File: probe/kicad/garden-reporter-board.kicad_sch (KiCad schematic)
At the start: 29 parts, among them J1 70543-0106, J2 Conn_01x02, J3 70543-0002, J4 70543-0002, J5 70543-0002, Q1 Q_NMOS_SGD, Q2 Q_PMOS_SGD, U1 MCP1700-3302E_TO92, U2 MCP1700-3302E_TO92, U3 MCP1700-1202E_TO92

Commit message: Finish and verifiy routing, finish and verify BOM
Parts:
- J5: value 70543-0002 -> 70543-0106
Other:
- moved on the sheet: C11, C6, C7, J4, Q1, Q2, R3, R6, U2

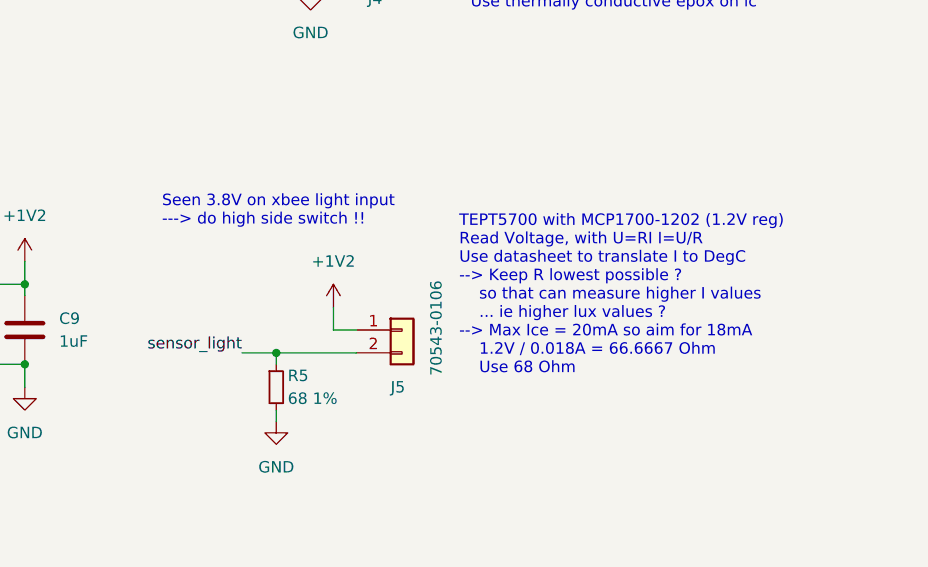
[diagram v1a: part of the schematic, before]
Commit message: High side switch working fine, fix few comments
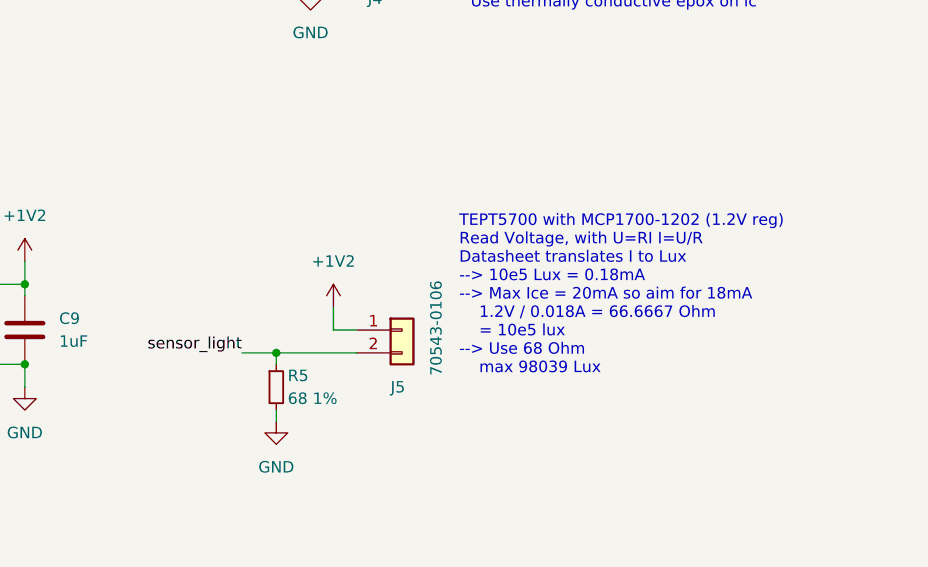
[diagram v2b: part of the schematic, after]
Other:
- note added: "TEPT5700 with MCP1700-1202 (1.2V reg) Read Voltage, with U=RI I=U/R Datasheet translates I to Lux --> 10e5 Lux = 0.18mA --> Max Ice = 20mA so aim for 18mA 1.2V / 0.018A = 66.6667 Ohm = 10e5 lux --> Use 68 Ohm max 98039 Lux"
- note removed: "Seen 3.8V on xbee light input ---> do high side switch !!"
- note removed: "TEPT5700 with MCP1700-1202 (1.2V reg) Read Voltage, with U=RI I=U/R Use datasheet to translate I to DegC --> Keep R lowest possible ? so that can measure higher I values ... ie higher lux values ? --> Max Ice = 20mA so aim for 18mA 1.2V / 0.018A = 66.6667 Ohm Use 68 Ohm"
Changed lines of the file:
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@@
-    (effects (font (size 1.27 1.27)) (justify left bottom))
-  )
-  (text "Seen 3.8V on xbee light input\n---> do high side switch !!"
-    (at 209.55 135.89 0)
     (effects (font (size 1.27 1.27)) (justify left bottom))
   )
@@
     (effects (font (size 1.27 1.27)) (justify left bottom))
   )
-  (text "TEPT5700 with MCP1700-1202 (1.2V reg)\nRead Voltage, with U=RI I=U/R\nUse datasheet to translate I to DegC\n--> Keep R lowest possible ?\n    so that can measure higher I values\n    ... ie higher lux values ?\n--> Max Ice = 20mA so aim for 18mA\n    1.2V / 0.018A = 66.6667 Ohm\n    Use 68 Ohm"
+  (text "TEPT5700 with MCP1700-1202 (1.2V reg)\nRead Voltage, with U=RI I=U/R\nDatasheet translates I to Lux\n--> 10e5 Lux = 0.18mA\n--> Max Ice = 20mA so aim for 18mA\n    1.2V / 0.018A = 66.6667 Ohm\n    = 10e5 lux\n--> Use 68 Ohm\n    max 98039 Lux"
     (at 242.57 152.4 0)
     (effects (font (size 1.27 1.27)) (justify left bottom))
